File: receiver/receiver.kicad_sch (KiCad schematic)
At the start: 0 parts

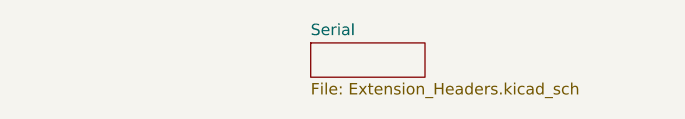
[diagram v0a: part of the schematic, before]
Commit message: restored v1.7 of receiver, since 2.0 is abandoned
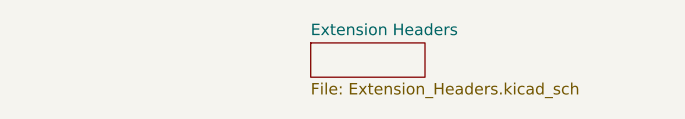
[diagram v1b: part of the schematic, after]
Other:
- sheet Serial renamed Extension Headers
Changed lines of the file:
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@@
 (kicad_sch
-	(version 20250114)
+	(version 20231120)
 	(generator "eeschema")
-	(generator_version "9.0")
+	(generator_version "8.0")
 	(paper "A4")
 	(sheet
 		(at 25.4 25.4)
 		(size 12.7 3.81)
-		(exclude_from_sim no)
-		(in_bom yes)
-		(on_board yes)
-		(dnp no)
 		(fields_autoplaced yes)
 		(stroke
@@
 		(at 177.8 25.4)
 		(size 12.7 3.81)
-		(exclude_from_sim no)
-		(in_bom yes)
-		(on_board yes)
-		(dnp no)
 		(fields_autoplaced yes)
 		(stroke
@@
 			(project "receiver"
 				(path "/778027c0-3525-441e-8e71-ce93a37417d3"
-					(page "5")
+					(page "4")
 				)
 			)
@@
 		(at 127 25.4)
 		(size 12.7 3.81)
-		(exclude_from_sim no)
-		(in_bom yes)
-		(on_board yes)
-		(dnp no)
 		(fields_autoplaced yes)
 		(stroke
@@
 			(project "receiver"
 				(path "/778027c0-3525-441e-8e71-ce93a37417d3"
-					(page "4")
+					(page "3")
 				)
 			)
@@
 		(at 76.2 25.4)
 		(size 12.7 3.81)
-		(exclude_from_sim no)
-		(in_bom yes)
-		(on_board yes)
-		(dnp no)
 		(fields_autoplaced yes)
 		(stroke
@@
 			(project "receiver"
 				(path "/778027c0-3525-441e-8e71-ce93a37417d3"
-					(page "3")
+					(page "2")
 				)
 			)
@@
 		(at 228.6 25.4)
 		(size 12.7 3.81)
-		(exclude_from_sim no)
-		(in_bom yes)
-		(on_board yes)
-		(dnp no)
 		(fields_autoplaced yes)
 		(stroke
@@
 			(color 0 0 0 0.0000)
 		)
-		(property "Sheetname" "Serial"
+		(property "Sheetname" "Extension Headers"
 			(at 228.6 24.6884 0)
 			(effects
@@
 			(project "receiver"
 				(path "/778027c0-3525-441e-8e71-ce93a37417d3"
-					(page "2")
+					(page "5")
 				)
 			)
@@
 		)
 	)
-	(embedded_fonts no)
 )
